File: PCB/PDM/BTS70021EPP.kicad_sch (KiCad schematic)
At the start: 12 parts, among them IC1 BTS70021EPPXUMA1

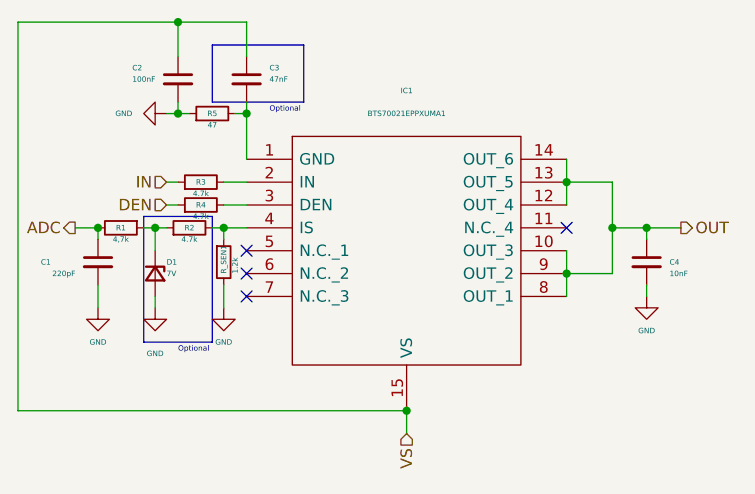
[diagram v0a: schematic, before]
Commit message: Added another high-side switch 2x7A + 2x4A SPI
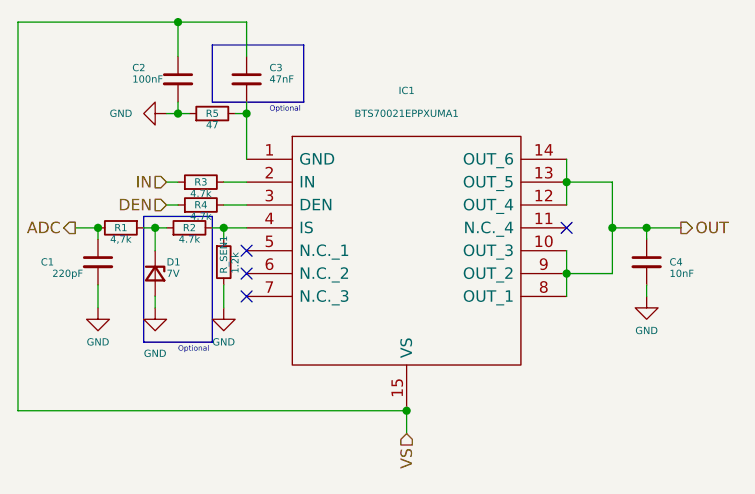
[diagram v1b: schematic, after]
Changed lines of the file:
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@@
     (in_bom yes) (on_board yes)
     (property "Reference" "C4" (id 0) (at 100.33 50.8 0)
-      (effects (font (size 0.6 0.6)) (justify left))
+      (effects (font (size 0.8 0.8)) (justify left))
     )
     (property "Value" "10nF" (id 1) (at 100.33 52.0762 0)
-      (effects (font (size 0.6 0.6)) (justify left))
+      (effects (font (size 0.8 0.8)) (justify left))
     )
     (property "Footprint" "Capacitor_SMD:C_0402_1005Metric" (id 2) (at 97.79 50.8 0)
@@
     (in_bom yes) (on_board yes)
     (property "Reference" "R4" (id 0) (at 48.26 44.45 90)
-      (effects (font (size 0.6 0.6)))
+      (effects (font (size 0.8 0.8)))
     )
     (property "Value" "4.7k" (id 1) (at 48.26 45.72 90)
-      (effects (font (size 0.6 0.6)))
+      (effects (font (size 0.8 0.8)))
     )
     (property "Footprint" "Resistor_SMD:R_0402_1005Metric" (id 2) (at 48.26 44.45 0)
@@
     (in_bom yes) (on_board yes)
     (property "Reference" "D1" (id 0) (at 44.45 50.8 90)
-      (effects (font (size 0.6 0.6)) (justify left))
+      (effects (font (size 0.8 0.8)) (justify left))
     )
     (property "Value" "7V" (id 1) (at 44.45 52.07 90)
-      (effects (font (size 0.6 0.6)) (justify left))
+      (effects (font (size 0.8 0.8)) (justify left))
     )
     (property "Footprint" "Diode_SMD:D_0805_2012Metric" (id 2) (at 43.18 52.07 90)
@@
     (in_bom yes) (on_board yes) (fields_autoplaced)
     (property "Reference" "#PWR03" (id 0) (at 38.1 34.29 0)
-      (effects (font (size 0.6 0.6)) hide)
+      (effects (font (size 0.8 0.8)) hide)
     )
     (property "Value" "GND" (id 1) (at 40.64 34.2899 90)
-      (effects (font (size 0.6 0.6)) (justify right))
+      (effects (font (size 0.8 0.8)) (justify right))
     )
     (property "Footprint" "" (id 2) (at 44.45 34.29 0)
@@
     (in_bom yes) (on_board yes)
     (property "Reference" "R1" (id 0) (at 39.37 46.99 90)
-      (effects (font (size 0.6 0.6)))
+      (effects (font (size 0.8 0.8)))
     )
     (property "Value" "4,7k" (id 1) (at 39.37 48.26 90)
-      (effects (font (size 0.6 0.6)))
+      (effects (font (size 0.8 0.8)))
     )
     (property "Footprint" "Resistor_SMD:R_0402_1005Metric" (id 2) (at 39.37 46.99 0)
@@
     (in_bom yes) (on_board yes)
     (property "Reference" "R_SEN1" (id 0) (at 50.8 52.07 90)
-      (effects (font (size 0.6 0.6)) (justify left))
+      (effects (font (size 0.8 0.8)) (justify left))
     )
     (property "Value" "1.2k" (id 1) (at 52.07 52.07 90)
-      (effects (font (size 0.6 0.6)) (justify left))
+      (effects (font (size 0.8 0.8)) (justify left))
     )
     (property "Footprint" "Resistor_SMD:R_0402_1005Metric" (id 2) (at 50.8 50.8 0)
@@
     (in_bom yes) (on_board yes)
     (property "Reference" "C2" (id 0) (at 40.64 29.21 0)
-      (effects (font (size 0.6 0.6)) (justify left))
+      (effects (font (size 0.8 0.8)) (justify left))
     )
     (property "Value" "100nF" (id 1) (at 40.64 30.48 0)
-      (effects (font (size 0.6 0.6)) (justify left))
+      (effects (font (size 0.8 0.8)) (justify left))
     )
     (property "Footprint" "Capacitor_SMD:C_0805_2012Metric" (id 2) (at 45.72 30.48 0)
@@
     (in_bom yes) (on_board yes) (fields_autoplaced)
     (property "Reference" "#PWR02" (id 0) (at 43.18 62.23 0)
-      (effects (font (size 0.6 0.6)) hide)
+      (effects (font (size 0.8 0.8)) hide)
     )
     (property "Value" "GND" (id 1) (at 43.18 60.96 0)
-      (effects (font (size 0.6 0.6)))
+      (effects (font (size 0.8 0.8)))
     )
     (property "Footprint" "" (id 2) (at 43.18 55.88 0)
@@
     (in_bom yes) (on_board yes) (fields_autoplaced)
     (property "Reference" "IC1" (id 0) (at 71.12 31.75 0)
-      (effects (font (size 0.6 0.6)))
+      (effects (font (size 0.8 0.8)))
     )
     (property "Value" "BTS70021EPPXUMA1" (id 1) (at 71.12 34.29 0)
-      (effects (font (size 0.6 0.6)))
+      (effects (font (size 0.8 0.8)))
     )
     (property "Footprint" "PDM_Additional:SOP65P600X115-15N" (id 2) (at 85.09 36.83 0)
@@
     (in_bom yes) (on_board yes)
     (property "Reference" "C3" (id 0) (at 55.88 29.21 0)
-      (effects (font (size 0.6 0.6)) (justify left))
+      (effects (font (size 0.8 0.8)) (justify left))
     )
     (property "Value" "47nF" (id 1) (at 55.88 30.48 0)
-      (effects (font (size 0.6 0.6)) (justify left))
+      (effects (font (size 0.8 0.8)) (justify left))
     )
     (property "Footprint" "Capacitor_SMD:C_0402_1005Metric" (id 2) (at 53.34 30.48 0)
@@
     (in_bom yes) (on_board yes)
     (property "Reference" "R3" (id 0) (at 48.26 41.91 90)
-      (effects (font (size 0.6 0.6)))
+      (effects (font (size 0.8 0.8)))
     )
     (property "Value" "4.7k" (id 1) (at 48.26 43.18 90)
-      (effects (font (size 0.6 0.6)))
+      (effects (font (size 0.8 0.8)))
     )
     (property "Footprint" "Resistor_SMD:R_0402_1005Metric" (id 2) (at 48.26 41.91 0)
@@
     (in_bom yes) (on_board yes)
     (property "Reference" "#PWR05" (id 0) (at 97.79 60.96 0)
-      (effects (font (size 0.6 0.6)) hide)
+      (effects (font (size 0.8 0.8)) hide)
     )
     (property "Value" "GND" (id 1) (at 97.79 58.42 0)
-      (effects (font (size 0.6 0.6)))
+      (effects (font (size 0.8 0.8)))
     )
     (property "Footprint" "" (id 2) (at 97.79 54.61 0)
@@
     (in_bom yes) (on_board yes)
     (property "Reference" "R5" (id 0) (at 49.53 34.29 90)
-      (effects (font (size 0.6 0.6)))
+      (effects (font (size 0.8 0.8)))
     )
     (property "Value" "47" (id 1) (at 49.53 35.56 90)
-      (effects (font (size 0.6 0.6)))
+      (effects (font (size 0.8 0.8)))
     )
     (property "Footprint" "Resistor_SMD:R_0402_1005Metric" (id 2) (at 49.53 34.29 0)
@@
     (in_bom yes) (on_board yes)
     (property "Reference" "#PWR04" (id 0) (at 50.8 62.23 0)
-      (effects (font (size 0.6 0.6)) hide)
+      (effects (font (size 0.8 0.8)) hide)
     )
     (property "Value" "GND" (id 1) (at 50.8 59.69 0)
-      (effects (font (size 0.6 0.6)))
+      (effects (font (size 0.8 0.8)))
     )
     (property "Footprint" "" (id 2) (at 50.8 55.88 0)
@@
     (in_bom yes) (on_board yes)
     (property "Reference" "C1" (id 0) (at 30.48 50.8 0)
-      (effects (font (size 0.6 0.6)) (justify left))
+      (effects (font (size 0.8 0.8)) (justify left))
     )
     (property "Value" "220pF" (id 1) (at 31.75 52.07 0)
-      (effects (font (size 0.6 0.6)) (justify left))
+      (effects (font (size 0.8 0.8)) (justify left))
     )
     (property "Footprint" "Capacitor_SMD:C_0402_1005Metric" (id 2) (at 36.83 50.8 0)
@@
     (in_bom yes) (on_board yes)
     (property "Reference" "#PWR01" (id 0) (at 36.83 62.23 0)
-      (effects (font (size 0.6 0.6)) hide)
+      (effects (font (size 0.8 0.8)) hide)
     )
     (property "Value" "GND" (id 1) (at 36.83 59.69 0)
-      (effects (font (size 0.6 0.6)))
+      (effects (font (size 0.8 0.8)))
     )
     (property "Footprint" "" (id 2) (at 36.83 55.88 0)
@@
     (in_bom yes) (on_board yes)
     (property "Reference" "R2" (id 0) (at 46.99 46.99 90)
-      (effects (font (size 0.6 0.6)))
+      (effects (font (size 0.8 0.8)))
     )
     (property "Value" "4.7k" (id 1) (at 46.99 48.26 90)
-      (effects (font (size 0.6 0.6)))
+      (effects (font (size 0.8 0.8)))
     )
     (property "Footprint" "Resistor_SMD:R_0402_1005Metric" (id 2) (at 46.99 46.99 0)

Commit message: Concept revision and MCU section changes
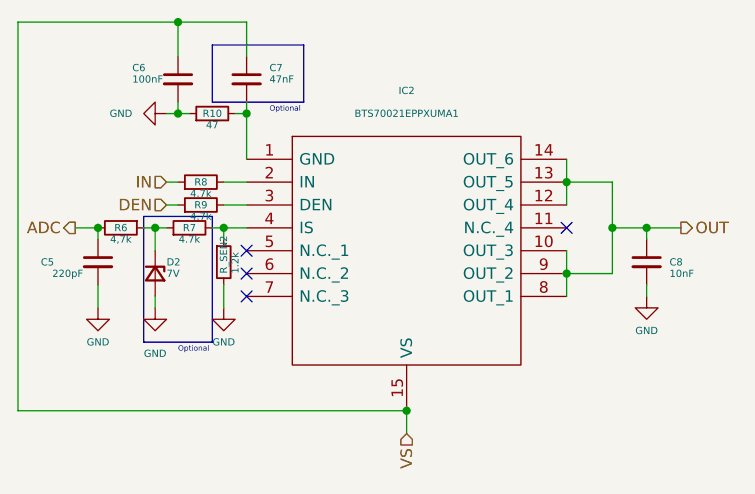
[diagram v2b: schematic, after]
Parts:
- renumbered C1 to C5, C2 to C6, C3 to C7, C4 to C8, D1 to D2, IC1 to IC2, R5 to R10, R1 to R6, R2 to R7, R3 to R8, R4 to R9, R_SEN1 to R_SEN2
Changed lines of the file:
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@@
   (symbol (lib_id "Device:C_Small") (at 97.79 50.8 0) (unit 1)
     (in_bom yes) (on_board yes)
-    (property "Reference" "C4" (id 0) (at 100.33 50.8 0)
+    (property "Reference" "C8" (id 0) (at 100.33 50.8 0)
       (effects (font (size 0.8 0.8)) (justify left))
     )
@@
   (symbol (lib_id "Device:R_Small") (at 48.26 44.45 90) (unit 1)
     (in_bom yes) (on_board yes)
-    (property "Reference" "R4" (id 0) (at 48.26 44.45 90)
+    (property "Reference" "R9" (id 0) (at 48.26 44.45 90)
       (effects (font (size 0.8 0.8)))
     )
@@
   (symbol (lib_id "Device:D_Zener_Small") (at 43.18 52.07 270) (unit 1)
     (in_bom yes) (on_board yes)
-    (property "Reference" "D1" (id 0) (at 44.45 50.8 90)
+    (property "Reference" "D2" (id 0) (at 44.45 50.8 90)
       (effects (font (size 0.8 0.8)) (justify left))
     )
@@
   (symbol (lib_id "power:GND") (at 44.45 34.29 270) (unit 1)
     (in_bom yes) (on_board yes) (fields_autoplaced)
-    (property "Reference" "#PWR03" (id 0) (at 38.1 34.29 0)
+    (property "Reference" "#PWR0102" (id 0) (at 38.1 34.29 0)
       (effects (font (size 0.8 0.8)) hide)
     )
@@
   (symbol (lib_id "Device:R_Small") (at 39.37 46.99 270) (unit 1)
     (in_bom yes) (on_board yes)
-    (property "Reference" "R1" (id 0) (at 39.37 46.99 90)
+    (property "Reference" "R6" (id 0) (at 39.37 46.99 90)
       (effects (font (size 0.8 0.8)))
     )
@@
   (symbol (lib_id "Device:R_Small") (at 50.8 50.8 0) (unit 1)
     (in_bom yes) (on_board yes)
-    (property "Reference" "R_SEN1" (id 0) (at 50.8 52.07 90)
+    (property "Reference" "R_SEN2" (id 0) (at 50.8 52.07 90)
       (effects (font (size 0.8 0.8)) (justify left))
     )
@@
   (symbol (lib_id "Device:C_Small") (at 45.72 30.48 0) (unit 1)
     (in_bom yes) (on_board yes)
-    (property "Reference" "C2" (id 0) (at 40.64 29.21 0)
+    (property "Reference" "C6" (id 0) (at 40.64 29.21 0)
       (effects (font (size 0.8 0.8)) (justify left))
     )
@@
   (symbol (lib_id "power:GND") (at 43.18 55.88 0) (unit 1)
     (in_bom yes) (on_board yes) (fields_autoplaced)
-    (property "Reference" "#PWR02" (id 0) (at 43.18 62.23 0)
+    (property "Reference" "#PWR0103" (id 0) (at 43.18 62.23 0)
       (effects (font (size 0.8 0.8)) hide)
     )
@@
   (symbol (lib_id "PDM_additional:BTS70021EPPXUMA1") (at 53.34 39.37 0) (unit 1)
     (in_bom yes) (on_board yes) (fields_autoplaced)
-    (property "Reference" "IC1" (id 0) (at 71.12 31.75 0)
+    (property "Reference" "IC2" (id 0) (at 71.12 31.75 0)
       (effects (font (size 0.8 0.8)))
     )
@@
   (symbol (lib_id "Device:C_Small") (at 53.34 30.48 0) (unit 1)
     (in_bom yes) (on_board yes)
-    (property "Reference" "C3" (id 0) (at 55.88 29.21 0)
+    (property "Reference" "C7" (id 0) (at 55.88 29.21 0)
       (effects (font (size 0.8 0.8)) (justify left))
     )
@@
   (symbol (lib_id "Device:R_Small") (at 48.26 41.91 90) (unit 1)
     (in_bom yes) (on_board yes)
-    (property "Reference" "R3" (id 0) (at 48.26 41.91 90)
+    (property "Reference" "R8" (id 0) (at 48.26 41.91 90)
       (effects (font (size 0.8 0.8)))
     )
@@
   (symbol (lib_id "power:GND") (at 97.79 54.61 0) (unit 1)
     (in_bom yes) (on_board yes)
-    (property "Reference" "#PWR05" (id 0) (at 97.79 60.96 0)
+    (property "Reference" "#PWR0105" (id 0) (at 97.79 60.96 0)
       (effects (font (size 0.8 0.8)) hide)
     )
@@
   (symbol (lib_id "Device:R_Small") (at 49.53 34.29 90) (unit 1)
     (in_bom yes) (on_board yes)
-    (property "Reference" "R5" (id 0) (at 49.53 34.29 90)
+    (property "Reference" "R10" (id 0) (at 49.53 34.29 90)
       (effects (font (size 0.8 0.8)))
     )
@@
   (symbol (lib_id "power:GND") (at 50.8 55.88 0) (unit 1)
     (in_bom yes) (on_board yes)
-    (property "Reference" "#PWR04" (id 0) (at 50.8 62.23 0)
+    (property "Reference" "#PWR0101" (id 0) (at 50.8 62.23 0)
       (effects (font (size 0.8 0.8)) hide)
     )
@@
   (symbol (lib_id "Device:C_Small") (at 36.83 50.8 0) (unit 1)
     (in_bom yes) (on_board yes)
-    (property "Reference" "C1" (id 0) (at 30.48 50.8 0)
+    (property "Reference" "C5" (id 0) (at 30.48 50.8 0)
       (effects (font (size 0.8 0.8)) (justify left))
     )
@@
   (symbol (lib_id "power:GND") (at 36.83 55.88 0) (unit 1)
     (in_bom yes) (on_board yes)
-    (property "Reference" "#PWR01" (id 0) (at 36.83 62.23 0)
+    (property "Reference" "#PWR0104" (id 0) (at 36.83 62.23 0)
       (effects (font (size 0.8 0.8)) hide)
     )
@@
   (symbol (lib_id "Device:R_Small") (at 46.99 46.99 90) (unit 1)
     (in_bom yes) (on_board yes)
-    (property "Reference" "R2" (id 0) (at 46.99 46.99 90)
-      (effects (font (size 0.8 0.8)))
-    )
+    (property "Reference" "R7" (id 0) (at 46.99 46.99 90)
+      (effects (font (size 0.8 0.8)))
+    )
